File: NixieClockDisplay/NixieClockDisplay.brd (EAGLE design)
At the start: 105.7 x 73 mm, 15 parts

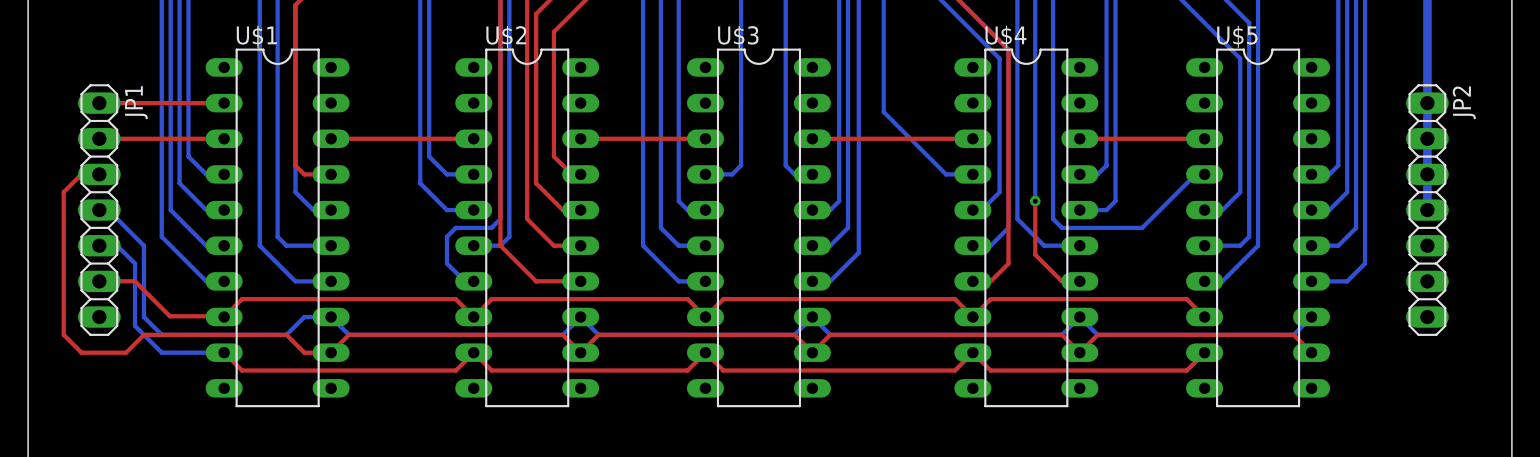
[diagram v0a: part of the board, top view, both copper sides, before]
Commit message: Flip the connection headers.
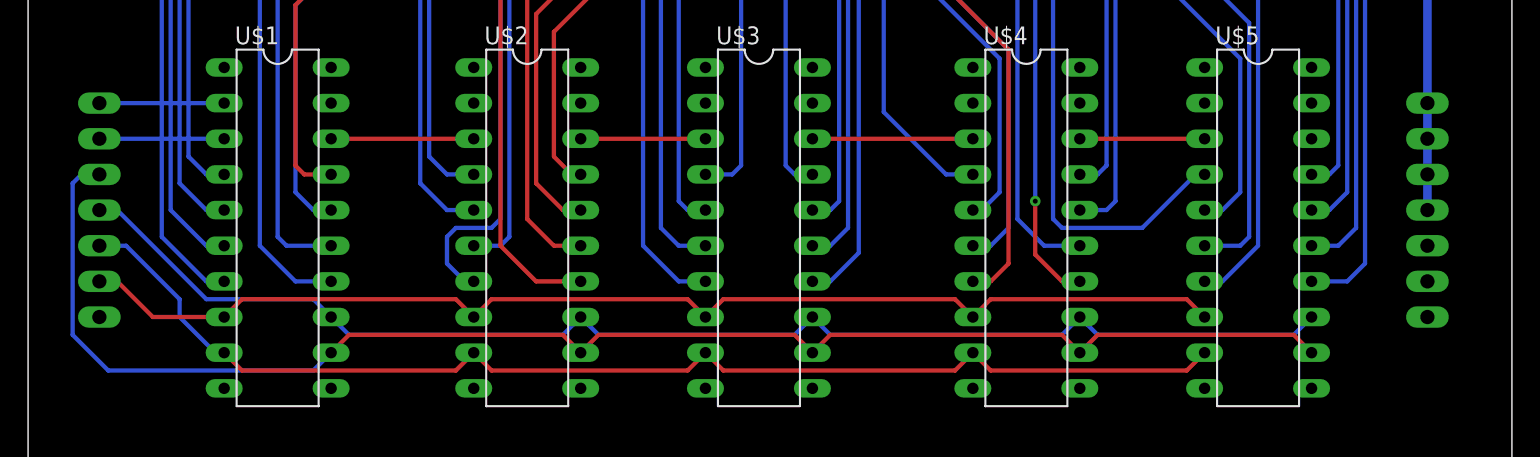
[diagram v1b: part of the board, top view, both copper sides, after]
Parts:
- flipped JP1 to the bottom
- flipped JP2 to the bottom
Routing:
- net SRCK: track 97.8 -> 93.7 mm
- net G: track 88.7 -> 86.8 mm
- net RCK: track 107.9 -> 107.0 mm
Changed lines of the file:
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@@
 <element name="U$4" library="ShiftRegister" package="DIL20" value="TPIC6B595" x="71.12" y="20.32" rot="R270"/>
 <element name="U$5" library="ShiftRegister" package="DIL20" value="TPIC6B595" x="87.63" y="20.32" rot="R270"/>
-<element name="JP1" library="pinhead" package="1X07" value="" x="5.08" y="21.59" rot="R270"/>
-<element name="JP2" library="pinhead" package="1X07" value="" x="99.695" y="21.59" rot="R270"/>
+<element name="JP1" library="pinhead" package="1X07" value="" x="5.08" y="21.59" rot="MR270"/>
+<element name="JP2" library="pinhead" package="1X07" value="" x="99.695" y="21.59" rot="MR270"/>
 </elements>
 <signals>
@@
 <wire x1="90.17" y1="12.7" x2="91.44" y2="11.43" width="0.3048" layer="1"/>
 <contactref element="JP1" pad="3"/>
-<wire x1="5.08" y1="24.13" x2="3.81" y2="24.13" width="0.3048" layer="1"/>
-<wire x1="3.81" y1="24.13" x2="2.54" y2="22.86" width="0.3048" layer="1"/>
-<wire x1="2.54" y1="22.86" x2="2.54" y2="12.7" width="0.3048" layer="1"/>
-<wire x1="2.54" y1="12.7" x2="3.81" y2="11.43" width="0.3048" layer="1"/>
-<wire x1="3.81" y1="11.43" x2="6.985" y2="11.43" width="0.3048" layer="1"/>
-<wire x1="6.985" y1="11.43" x2="8.255" y2="12.7" width="0.3048" layer="1"/>
-<wire x1="8.255" y1="12.7" x2="18.415" y2="12.7" width="0.3048" layer="1"/>
-<wire x1="18.415" y1="12.7" x2="19.685" y2="11.43" width="0.3048" layer="1"/>
-<wire x1="19.685" y1="11.43" x2="21.59" y2="11.43" width="0.3048" layer="1"/>
+<wire x1="5.08" y1="24.13" x2="3.81" y2="24.13" width="0.3048" layer="16"/>
+<wire x1="3.81" y1="24.13" x2="3.175" y2="23.495" width="0.3048" layer="16"/>
+<wire x1="3.175" y1="23.495" x2="3.175" y2="12.7" width="0.3048" layer="16"/>
+<wire x1="3.175" y1="12.7" x2="5.715" y2="10.16" width="0.3048" layer="16"/>
+<wire x1="5.715" y1="10.16" x2="20.32" y2="10.16" width="0.3048" layer="16"/>
+<wire x1="20.32" y1="10.16" x2="21.59" y2="11.43" width="0.3048" layer="16"/>
 </signal>
 <signal name="SRCK">
@@
 <wire x1="90.17" y1="12.7" x2="91.44" y2="13.97" width="0.3048" layer="16"/>
 <contactref element="JP1" pad="4"/>
-<wire x1="5.08" y1="21.59" x2="5.715" y2="21.59" width="0.3048" layer="16"/>
-<wire x1="5.715" y1="21.59" x2="8.255" y2="19.05" width="0.3048" layer="16"/>
-<wire x1="8.255" y1="19.05" x2="8.255" y2="13.97" width="0.3048" layer="16"/>
-<wire x1="8.255" y1="13.97" x2="9.525" y2="12.7" width="0.3048" layer="16"/>
-<wire x1="9.525" y1="12.7" x2="18.415" y2="12.7" width="0.3048" layer="16"/>
-<wire x1="18.415" y1="12.7" x2="19.685" y2="13.97" width="0.3048" layer="16"/>
-<wire x1="19.685" y1="13.97" x2="21.59" y2="13.97" width="0.3048" layer="16"/>
+<wire x1="5.08" y1="21.59" x2="6.35" y2="21.59" width="0.3048" layer="16"/>
+<wire x1="6.35" y1="21.59" x2="12.7" y2="15.24" width="0.3048" layer="16"/>
+<wire x1="20.32" y1="15.24" x2="21.59" y2="13.97" width="0.3048" layer="16"/>
+<wire x1="12.7" y1="15.24" x2="20.32" y2="15.24" width="0.3048" layer="16"/>
 </signal>
 <signal name="G">
@@
 <wire x1="82.55" y1="10.16" x2="83.82" y2="11.43" width="0.3048" layer="1"/>
 <contactref element="JP1" pad="5"/>
-<wire x1="5.08" y1="19.05" x2="6.35" y2="19.05" width="0.3048" layer="16"/>
-<wire x1="6.35" y1="19.05" x2="7.62" y2="17.78" width="0.3048" layer="16"/>
-<wire x1="7.62" y1="17.78" x2="7.62" y2="13.335" width="0.3048" layer="16"/>
-<wire x1="7.62" y1="13.335" x2="9.525" y2="11.43" width="0.3048" layer="16"/>
-<wire x1="9.525" y1="11.43" x2="13.97" y2="11.43" width="0.3048" layer="16"/>
+<wire x1="5.08" y1="19.05" x2="6.985" y2="19.05" width="0.3048" layer="16"/>
+<wire x1="6.985" y1="19.05" x2="10.795" y2="15.24" width="0.3048" layer="16"/>
+<wire x1="10.795" y1="15.24" x2="10.795" y2="13.97" width="0.3048" layer="16"/>
+<wire x1="10.795" y1="13.97" x2="13.335" y2="11.43" width="0.3048" layer="16"/>
+<wire x1="13.335" y1="11.43" x2="13.97" y2="11.43" width="0.3048" layer="16"/>
 </signal>
 <signal name="SRCCLR">
@@
 <contactref element="U$4" pad="!SRCLR"/>
 <contactref element="U$5" pad="!SRCLR"/>
-<wire x1="14.022553125" y1="14.022553125" x2="13.97" y2="13.97" width="0.3048" layer="1"/>
-<wire x1="14.022553125" y1="14.022553125" x2="15.24" y2="15.24" width="0.3048" layer="1"/>
-<wire x1="15.24" y1="15.24" x2="30.48" y2="15.24" width="0.3048" layer="1"/>
-<wire x1="30.48" y1="15.24" x2="31.75" y2="13.97" width="0.3048" layer="1"/>
 <wire x1="31.75" y1="13.97" x2="33.02" y2="15.24" width="0.3048" layer="1"/>
 <wire x1="33.02" y1="15.24" x2="46.99" y2="15.24" width="0.3048" layer="1"/>
@@
 <wire x1="82.55" y1="15.24" x2="83.82" y2="13.97" width="0.3048" layer="1"/>
 <contactref element="JP1" pad="6"/>
-<wire x1="5.08" y1="16.51" x2="7.62" y2="16.51" width="0.3048" layer="1"/>
-<wire x1="7.62" y1="16.51" x2="10.107446875" y2="14.022553125" width="0.3048" layer="1"/>
-<wire x1="10.107446875" y1="14.022553125" x2="14.022553125" y2="14.022553125" width="0.3048" layer="1"/>
+<wire x1="13.97" y1="13.97" x2="15.24" y2="15.24" width="0.3048" layer="1"/>
+<wire x1="15.24" y1="15.24" x2="30.48" y2="15.24" width="0.3048" layer="1"/>
+<wire x1="30.48" y1="15.24" x2="31.75" y2="13.97" width="0.3048" layer="1"/>
+<wire x1="5.08" y1="16.51" x2="6.35" y2="16.51" width="0.3048" layer="1"/>
+<wire x1="6.35" y1="16.51" x2="8.89" y2="13.97" width="0.3048" layer="1"/>
+<wire x1="8.89" y1="13.97" x2="13.97" y2="13.97" width="0.3048" layer="1"/>
 </signal>
 <signal name="GND">
@@
 <contactref element="U$5" pad="VCC"/>
 <contactref element="JP1" pad="1"/>
-<wire x1="5.08" y1="29.21" x2="13.97" y2="29.21" width="0.3048" layer="1"/>
+<wire x1="5.08" y1="29.21" x2="13.97" y2="29.21" width="0.3048" layer="16"/>
 <wire x1="67.31" y1="29.21" x2="83.82" y2="29.21" width="0" layer="19" extent="1-1"/>
 <wire x1="48.26" y1="29.21" x2="67.31" y2="29.21" width="0" layer="19" extent="1-1"/>
@@
 <contactref element="U$1" pad="SERIN"/>
 <contactref element="JP1" pad="2"/>
-<wire x1="5.08" y1="26.67" x2="13.97" y2="26.67" width="0.3048" layer="1"/>
+<wire x1="5.08" y1="26.67" x2="13.97" y2="26.67" width="0.3048" layer="16"/>
 </signal>
 </signals>

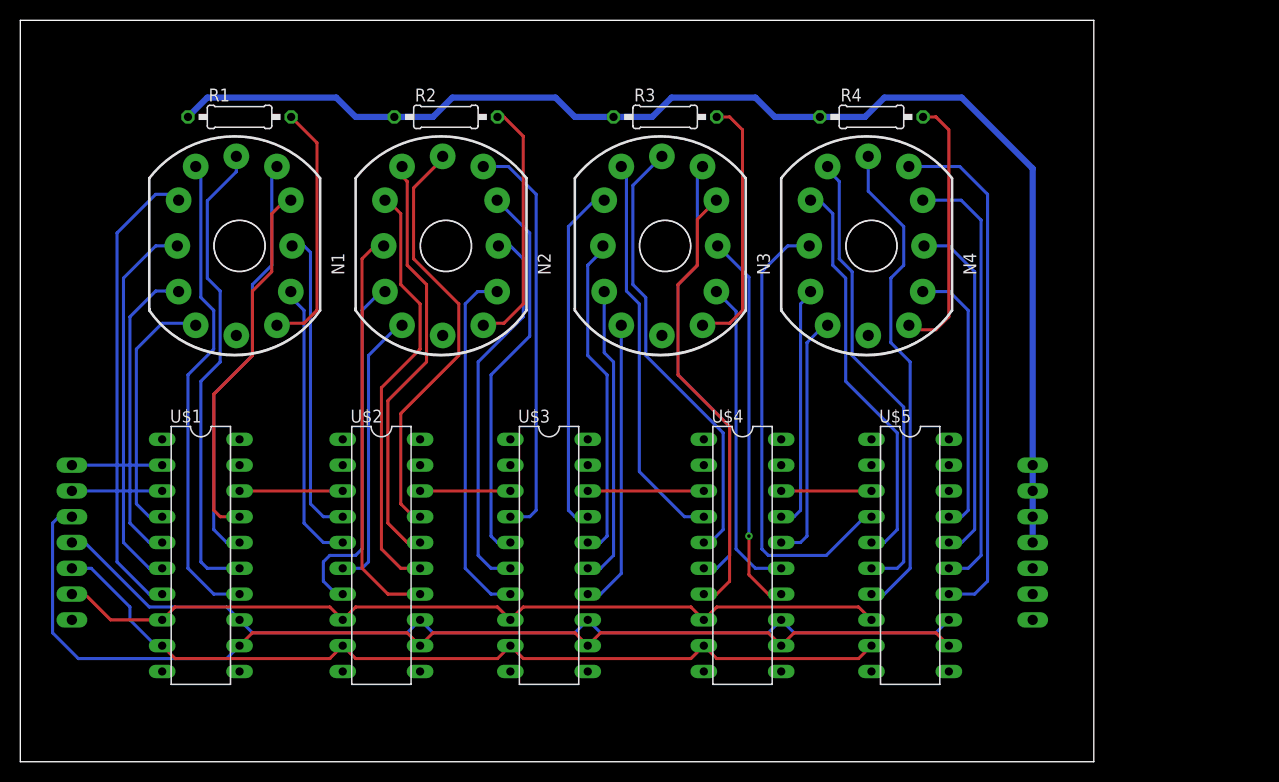
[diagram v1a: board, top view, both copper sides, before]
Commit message: Spread out the tubes more. Fix up some traces. Add ground pours.
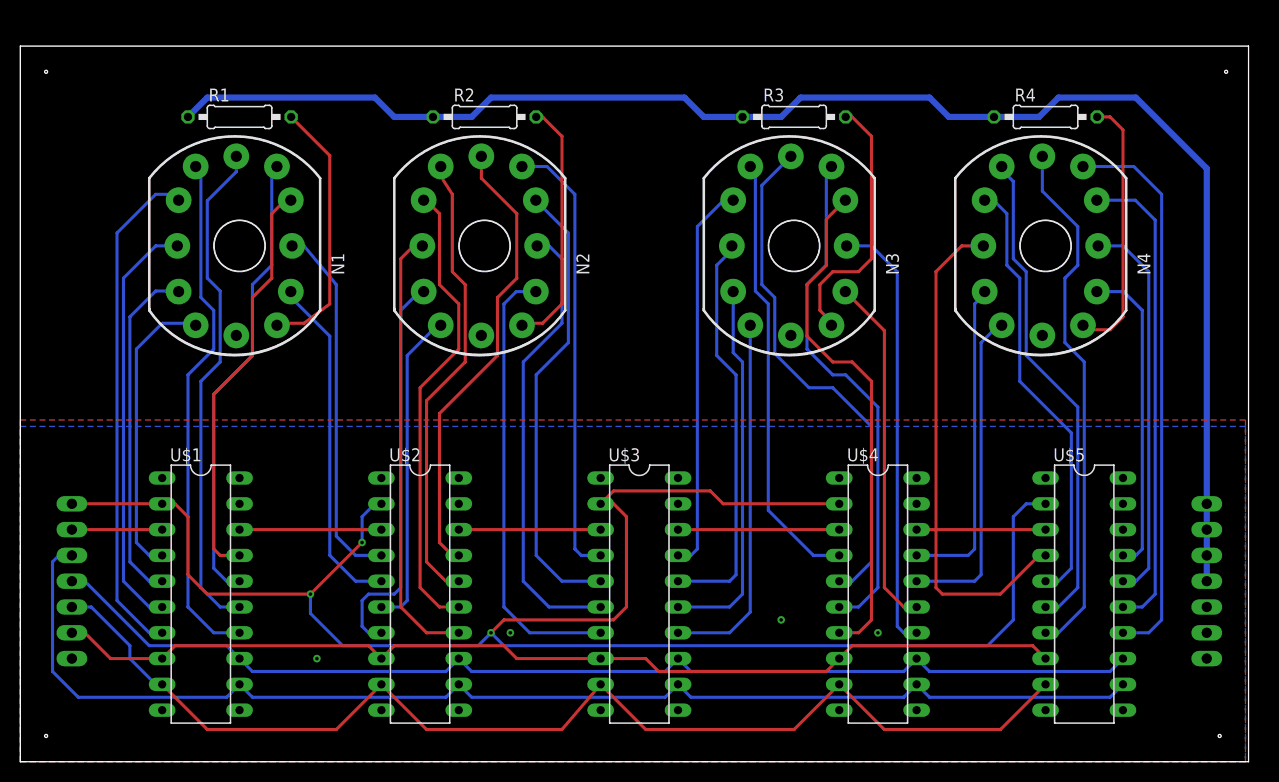
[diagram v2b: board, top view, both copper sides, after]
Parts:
- moved JP2 17.6 mm to (116.8, 17.8)
- moved U$5 17.6 mm to (104.8, 16.5)
- moved N4 17.1 mm to (101.0, 50.8)
- moved R4 17.1 mm to (101.0, 63.5)
- moved U$4 13.9 mm to (84.5, 16.5)
- moved N3 12.7 mm to (76.2, 50.8)
- moved R3 12.7 mm to (76.2, 63.5)
- moved U$3 9.67 mm to (61.0, 16.5)
- moved U$2 5.39 mm to (39.4, 16.5)
- moved N2 3.81 mm to (45.7, 50.8)
- moved R2 3.81 mm to (45.7, 63.5)
- moved JP1 3.81 mm to (5.08, 17.8)
- moved U$1 3.81 mm to (17.8, 16.5)
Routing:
- net VCC: track 8.89 -> 182.0 mm, vias 0 -> 3
- net G: track 86.8 -> 114.7 mm
- net HV: track 128.4 -> 149.4 mm
- net SRCK: track 93.7 -> 110.9 mm
- net SRCCLR: track 84.0 -> 101.1 mm
- net RCK: track 107.0 -> 124.2 mm
- net N$24: track 35.2 -> 44.1 mm
- net N$27: track 32.2 -> 39.8 mm
- net N$36: track 24.1 -> 31.7 mm
- net N$25: track 28.6 -> 36.2 mm
- net N$26: track 29.4 -> 37.0 mm
- net N$35: track 24.6 -> 32.2 mm
- net N$23: track 37.7 -> 45.0 mm
- net N$22: track 38.1 -> 45.0 mm
- net N$30: track 44.1 -> 50.9 mm
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- added copper zone on layer 1, net GND
- added copper zone on layer 16, net GND
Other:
- board size 105.7 x 73 mm -> 121 x 70.5 mm

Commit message: Fix up spacing. Change mounting holes to vias.
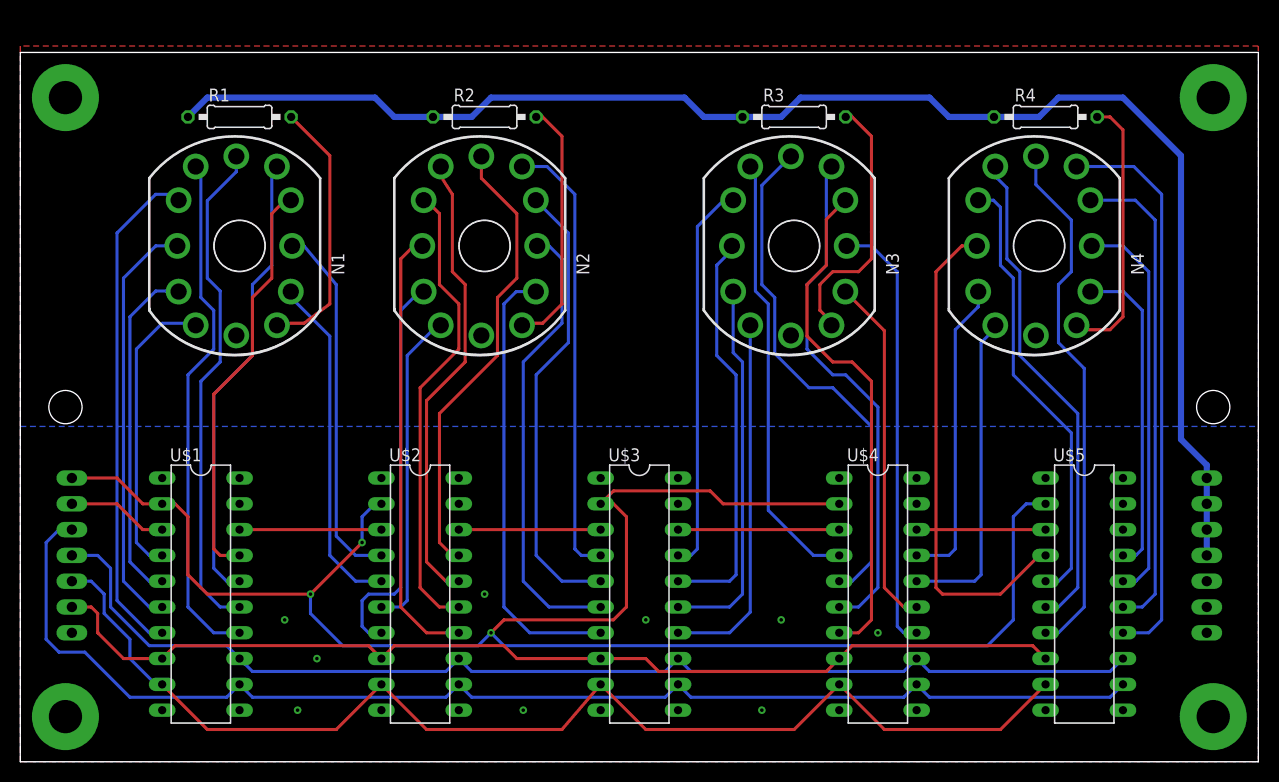
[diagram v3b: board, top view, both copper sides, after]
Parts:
- moved JP1 2.54 mm to (5.08, 20.3)
- moved JP2 2.54 mm to (116.8, 20.3)
- moved N4 0.64 mm to (100.3, 50.8)
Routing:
- net SRCK: track 110.9 -> 114.2 mm
- net HV: track 149.4 -> 146.1 mm
- net G: track 114.7 -> 117.3 mm
- net SRCCLR: track 101.1 -> 103.3 mm
- net RCK: track 124.2 -> 125.7 mm
- net N$36: track 31.7 -> 30.4 mm
- net VCC: track 182.0 -> 183.0 mm
- net SERIN: track 8.89 -> 9.94 mm
- net N$44: track 30.9 -> 31.5 mm
- net N$43: track 38.3 -> 38.9 mm
- net N$42: track 47.1 -> 47.7 mm
- net N$38: track 43.4 -> 44.0 mm
- net N$41: track 55.1 -> 55.8 mm
- net N$37: track 49.5 -> 48.8 mm
- net N$4: track 26.1 -> 26.7 mm
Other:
- board size 121 x 70.5 mm -> 121.9 x 69.8 mm
